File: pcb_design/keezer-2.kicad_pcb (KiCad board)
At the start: 2 copper layers, 27.9 x 39.4 mm, 10 parts, among them Q1 PN2222A, T1 CONN_01X03_FEMALE, T2 CONN_01X03_FEMALE, T3 CONN_01X03_FEMALE

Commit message: Wire everything up in the pcb
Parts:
- moved R2 12.7 mm to (172.7, 129.5)
- moved Q1 2.84 mm to (156.2, 119.4), turned to 90 degrees
- moved R1 2.54 mm to (158.8, 130.8)
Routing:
- net GND: track 0.00 -> 96.1 mm
- net +3V3: track 0.00 -> 88.0 mm
- net BCM4: track 0.00 -> 68.6 mm, vias 0 -> 1
- net +5V: track 0.00 -> 38.2 mm
- net SCL: track 0.00 -> 29.0 mm
- net SDA: track 0.00 -> 25.7 mm
- net RELAY_OUT: track 0.00 -> 16.6 mm
- net BCM17: track 0.00 -> 10.7 mm
- net TRANSISTOR_BASE: track 0.00 -> 8.89 mm
- removed copper zone on F.Cu, net +3V3
- removed copper zone on F.Cu, net +5V
- removed copper zone on B.Cu, net GND
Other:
- board size 27.9 x 39.4 mm -> 29.2 x 39.4 mm
- rule trace_min: 0.2 -> 0.1524

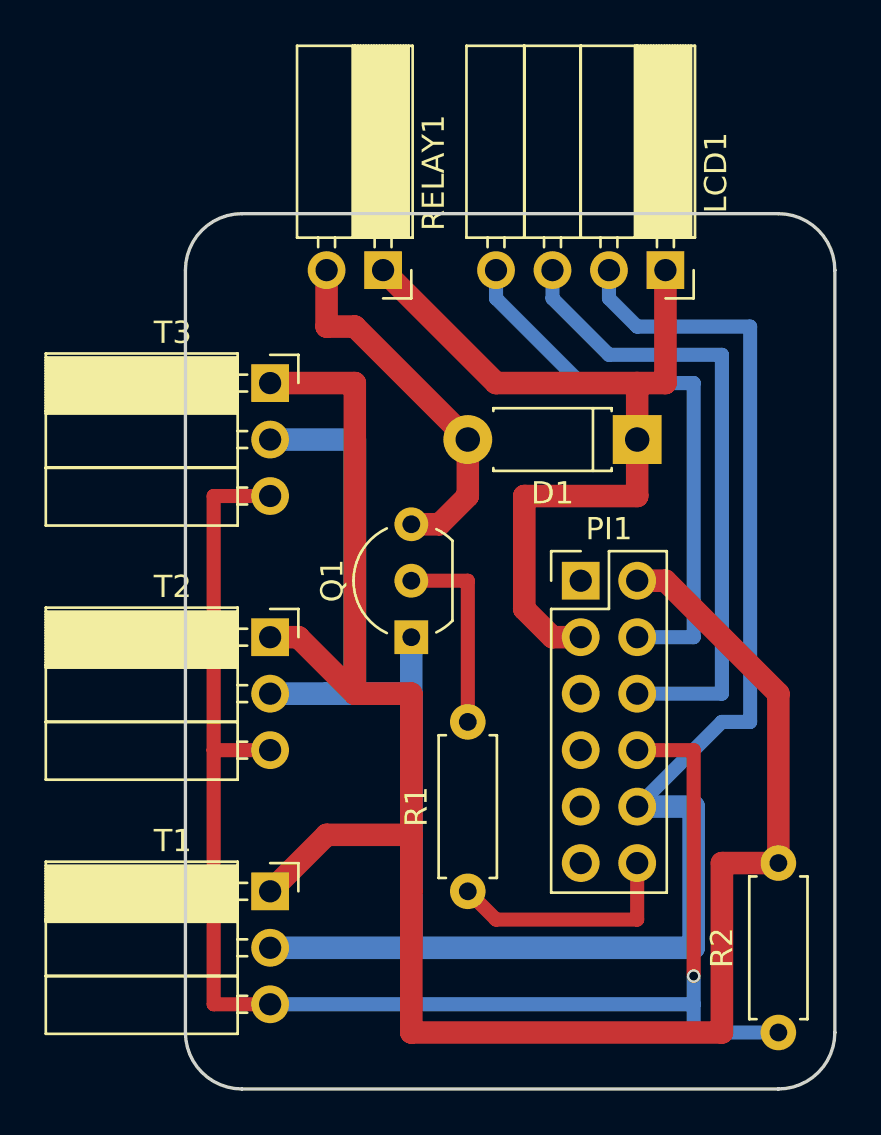
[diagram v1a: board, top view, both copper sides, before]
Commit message: Fix some silkscreen; fill bottom layer with ground zone
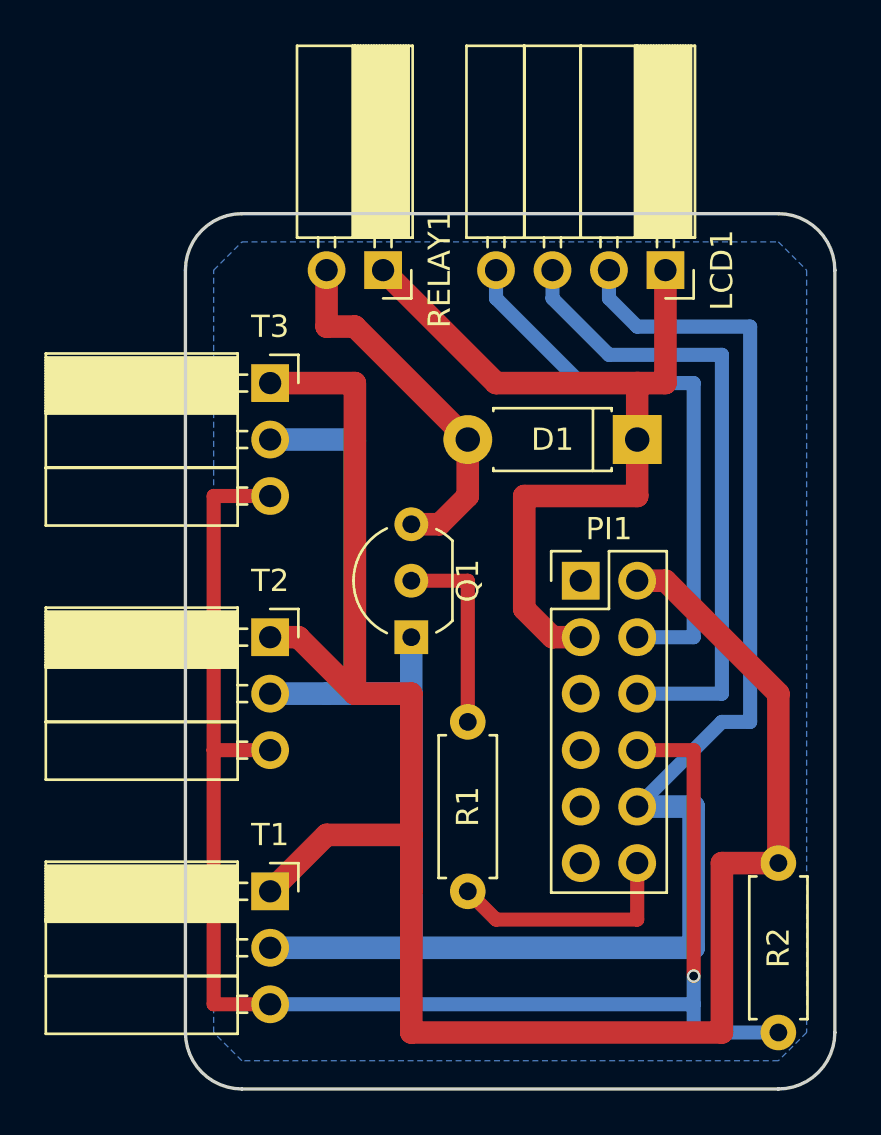
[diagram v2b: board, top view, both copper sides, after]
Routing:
- added copper zone on B.Cu, net GND
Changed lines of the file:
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@@
     (links 22)
     (no_connects 0)
-    (area 137.327619 90.337618 175.335001 139.775001)
+    (area 145.974999 100.254999 175.335001 139.775001)
     (thickness 1.6)
     (drawings 8)
@@
   (layers
     (0 F.Cu signal)
-    (31 B.Cu signal hide)
+    (31 B.Cu signal)
     (32 B.Adhes user)
     (33 F.Adhes user)
@@
     (pad_to_mask_clearance 0.2)
     (aux_axis_origin 0 0)
-    (visible_elements 7FFCFFFF)
+    (visible_elements 7FFEFFFF)
     (pcbplotparams
       (layerselection 0x00030_80000001)
@@
     (descr "D, DO-41_SOD81 series, Axial, Horizontal, pin pitch=7.62mm, , length*diameter=5.2*2.7mm^2, , http://www.diodes.com/_files/packages/DO-41%20(Plastic).pdf")
     (tags "D DO-41_SOD81 series Axial Horizontal pin pitch 7.62mm  length 5.2mm diameter 2.7mm")
-    (fp_text reference D1 (at 3.81 -2.41 180) (layer F.SilkS)
+    (fp_text reference D1 (at 3.81 0 180) (layer F.SilkS)
       (effects (font (size 1 1) (thickness 0.15)))
     )
@@
     (descr "Through hole angled socket strip, 1x04, 2.54mm pitch, 8.51mm socket length, single row")
     (tags "Through hole angled socket strip THT 1x04 2.54mm single row")
-    (fp_text reference LCD1 (at -4.38 -2.27 270) (layer F.SilkS)
+    (fp_text reference LCD1 (at 0 -2.54 270) (layer F.SilkS)
       (effects (font (size 1 1) (thickness 0.15)))
     )
@@
     (descr "TO-92 leads in-line, wide, drill 0.8mm (see NXP sot054_po.pdf)")
     (tags "to-92 sc-43 sc-43a sot54 PA33 transistor")
-    (fp_text reference Q1 (at 2.54 -3.56 270) (layer F.SilkS)
+    (fp_text reference Q1 (at 2.54 2.54 270) (layer F.SilkS)
       (effects (font (size 1 1) (thickness 0.15)))
     )
@@
       (effects (font (size 1 1) (thickness 0.15)))
     )
-    (fp_text user %R (at 2.54 -3.56 270) (layer F.Fab)
+    (fp_text user %R (at 2.54 2.54 270) (layer F.Fab)
       (effects (font (size 1 1) (thickness 0.15)))
     )
@@
     (descr "Resistor, Axial_DIN0207 series, Axial, Horizontal, pin pitch=7.62mm, 0.25W = 1/4W, length*diameter=6.3*2.5mm^2, http://cdn-reichelt.de/documents/datenblatt/B400/1_4W%23YAG.pdf")
     (tags "Resistor Axial_DIN0207 series Axial Horizontal pin pitch 7.62mm 0.25W = 1/4W length 6.3mm diameter 2.5mm")
-    (fp_text reference R1 (at 3.81 -2.31 90) (layer F.SilkS)
+    (fp_text reference R1 (at 3.81 0 90) (layer F.SilkS)
       (effects (font (size 1 1) (thickness 0.15)))
     )
@@
     (descr "Resistor, Axial_DIN0207 series, Axial, Horizontal, pin pitch=7.62mm, 0.25W = 1/4W, length*diameter=6.3*2.5mm^2, http://cdn-reichelt.de/documents/datenblatt/B400/1_4W%23YAG.pdf")
     (tags "Resistor Axial_DIN0207 series Axial Horizontal pin pitch 7.62mm 0.25W = 1/4W length 6.3mm diameter 2.5mm")
-    (fp_text reference R2 (at 3.81 2.54 270) (layer F.SilkS)
+    (fp_text reference R2 (at 3.81 0 270) (layer F.SilkS)
       (effects (font (size 1 1) (thickness 0.15)))
     )
@@
     (descr "Through hole angled socket strip, 1x02, 2.54mm pitch, 8.51mm socket length, single row")
     (tags "Through hole angled socket strip THT 1x02 2.54mm single row")
-    (fp_text reference RELAY1 (at -4.38 -2.27 270) (layer F.SilkS)
+    (fp_text reference RELAY1 (at 0 -2.54 270) (layer F.SilkS)
       (effects (font (size 1 1) (thickness 0.15)))
     )
@@
     (descr "Through hole angled socket strip, 1x03, 2.54mm pitch, 8.51mm socket length, single row")
     (tags "Through hole angled socket strip THT 1x03 2.54mm single row")
-    (fp_text reference T1 (at -4.38 -2.27) (layer F.SilkS)
+    (fp_text reference T1 (at 0 -2.54) (layer F.SilkS)
       (effects (font (size 1 1) (thickness 0.15)))
     )
@@
     (descr "Through hole angled socket strip, 1x03, 2.54mm pitch, 8.51mm socket length, single row")
     (tags "Through hole angled socket strip THT 1x03 2.54mm single row")
-    (fp_text reference T2 (at -4.38 -2.27) (layer F.SilkS)
+    (fp_text reference T2 (at 0 -2.54) (layer F.SilkS)
       (effects (font (size 1 1) (thickness 0.15)))
     )
@@
     (descr "Through hole angled socket strip, 1x03, 2.54mm pitch, 8.51mm socket length, single row")
     (tags "Through hole angled socket strip THT 1x03 2.54mm single row")
-    (fp_text reference T3 (at -4.38 -2.27) (layer F.SilkS)
+    (fp_text reference T3 (at 0 -2.54) (layer F.SilkS)
       (effects (font (size 1 1) (thickness 0.15)))
     )
@@
   (segment (start 157.48 114.3) (end 158.75 113.03) (width 1.016) (layer F.Cu) (net 2))
   (segment (start 153.67 121.92) (end 153.67 110.49) (width 1.016) (layer B.Cu) (net 3))
-  (segment (start 153.67 110.49) (end 149.86 110.49) (width 1.016) (layer B.Cu) (net 3) (status 800000))
+  (segment (start 153.67 110.49) (end 149.86 110.49) (width 1.016) (layer B.Cu) (net 3))
   (segment (start 156.21 121.92) (end 156.21 133.35) (width 1.016) (layer B.Cu) (net 3))
   (segment (start 149.86 121.92) (end 152.4 121.92) (width 1.016) (layer B.Cu) (net 3))
@@
   (segment (start 172.72 121.92) (end 172.72 129.54) (width 1.016) (layer F.Cu) (net 6))
   (segment (start 167.64 116.84) (end 172.72 121.92) (width 1.016) (layer F.Cu) (net 6))
-  (segment (start 147.32 124.46) (end 149.86 124.46) (width 0.635) (layer F.Cu) (net 9) (status 800000))
-  (segment (start 149.86 135.89) (end 168.91 135.89) (width 0.635) (layer B.Cu) (net 9) (status 400000))
-  (segment (start 149.86 135.89) (end 147.32 135.89) (width 0.635) (layer F.Cu) (net 9) (status 400000))
-  (segment (start 147.32 113.03) (end 149.86 113.03) (width 0.635) (layer F.Cu) (net 9) (status 800000))
+  (segment (start 147.32 124.46) (end 149.86 124.46) (width 0.635) (layer F.Cu) (net 9))
+  (segment (start 149.86 135.89) (end 168.91 135.89) (width 0.635) (layer B.Cu) (net 9))
+  (segment (start 149.86 135.89) (end 147.32 135.89) (width 0.635) (layer F.Cu) (net 9))
+  (segment (start 147.32 113.03) (end 149.86 113.03) (width 0.635) (layer F.Cu) (net 9))
   (segment (start 147.32 135.89) (end 147.32 124.46) (width 0.635) (layer F.Cu) (net 9))
   (segment (start 147.32 124.46) (end 147.32 113.03) (width 0.635) (layer F.Cu) (net 9))
@@
   (segment (start 158.75 123.19) (end 158.75 116.84) (width 0.635) (layer F.Cu) (net 13))
   (segment (start 158.75 116.84) (end 156.21 116.84) (width 0.635) (layer F.Cu) (net 13))
+  (zone (net 3) (net_name GND) (layer B.Cu) (hatch edge 0.508)
+    (connect_pads (clearance 0.508))
+    (min_thickness 0.254)
+    (fill yes (arc_segments 16) (thermal_gap 0.508) (thermal_bridge_width 0.508))
+    (polygon
+      (pts
+        (xy 173.99 102.87) (xy 173.99 137.16) (xy 172.72 138.43) (xy 148.59 138.43) (xy 147.32 137.16)
+        (xy 147.32 102.87) (xy 148.59 101.6) (xy 172.72 101.6)
+      )
+    )
+  )
 )

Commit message: Add more silkscreen
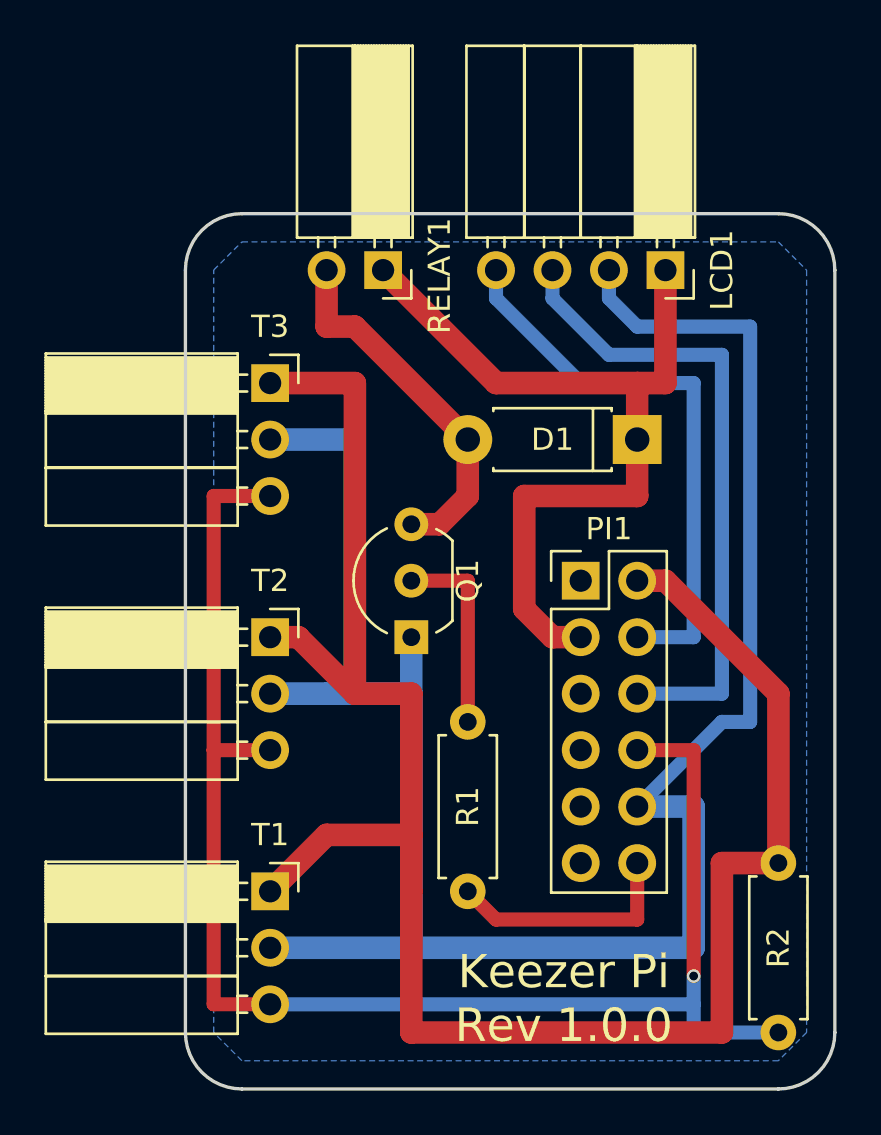
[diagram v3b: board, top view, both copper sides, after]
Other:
- board text added: "+"
- board text added: "+5v"
- board text added: "-"
- board text added: "DQ"
- board text added: "GND"
- board text added: "Keezer Pi Rev 1.0.0"
- board text added: "LCD1"
- board text added: "RELAY1"
- board text added: "SCL"
- board text added: "SDA"
- board text added: "T1"
- board text added: "T2"
- board text added: "T3"
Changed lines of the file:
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@@
     (area 145.974999 100.254999 175.335001 139.775001)
     (thickness 1.6)
-    (drawings 8)
+    (drawings 29)
     (tracks 77)
     (zones 0)
@@
   )
   (setup
-    (last_trace_width 1.016)
+    (last_trace_width 0.25)
     (user_trace_width 0.254)
     (user_trace_width 0.635)
@@
     (descr "Through hole angled socket strip, 1x02, 2.54mm pitch, 8.51mm socket length, single row")
     (tags "Through hole angled socket strip THT 1x02 2.54mm single row")
-    (fp_text reference RELAY1 (at 0 -2.54 270) (layer F.SilkS)
+    (fp_text reference RELAY1 (at 0.254 -2.54 270) (layer F.SilkS)
       (effects (font (size 1 1) (thickness 0.15)))
     )
@@
     (fp_line (start -10.55 4.35) (end -10.55 -1.8) (layer F.CrtYd) (width 0.05))
     (fp_line (start -10.55 -1.8) (end 1.8 -1.8) (layer F.CrtYd) (width 0.05))
-    (fp_text user %R (at 0 -2.54 270) (layer F.Fab)
+    (fp_text user %R (at 0.254 -2.54 270) (layer F.Fab)
       (effects (font (size 1 1) (thickness 0.15)))
     )
@@
     )
   )
+  (gr_text T1 (at 149.86 128.27) (layer B.SilkS)
+    (effects (font (size 1.016 1.016) (thickness 0.127)) (justify mirror))
+  )
+  (gr_text T2 (at 149.86 116.84) (layer B.SilkS)
+    (effects (font (size 1.016 1.016) (thickness 0.127)) (justify mirror))
+  )
+  (gr_text T3 (at 149.86 105.41) (layer B.SilkS)
+    (effects (font (size 1.016 1.016) (thickness 0.127)) (justify mirror))
+  )
+  (gr_text RELAY1 (at 157.48 103.124 90) (layer B.SilkS)
+    (effects (font (size 1.016 1.016) (thickness 0.127)) (justify mirror))
+  )
+  (gr_text "LCD1\n" (at 171.196 102.87) (layer B.SilkS)
+    (effects (font (size 1.016 1.016) (thickness 0.127)) (justify mirror))
+  )
+  (gr_text "Keezer Pi\nRev 1.0.0" (at 163.068 135.636) (layer F.SilkS)
+    (effects (font (size 1.5 1.5) (thickness 0.3)))
+  )
+  (gr_text DQ (at 151.638 135.89) (layer B.SilkS)
+    (effects (font (size 0.762 0.762) (thickness 0.1524)) (justify mirror))
+  )
+  (gr_text - (at 151.638 133.35) (layer B.SilkS)
+    (effects (font (size 0.762 0.762) (thickness 0.1524)) (justify mirror))
+  )
+  (gr_text + (at 151.638 130.81) (layer B.SilkS)
+    (effects (font (size 0.762 0.762) (thickness 0.1524)) (justify mirror))
+  )
+  (gr_text DQ (at 151.638 124.46) (layer B.SilkS)
+    (effects (font (size 0.762 0.762) (thickness 0.1524)) (justify mirror))
+  )
+  (gr_text - (at 151.638 121.92) (layer B.SilkS)
+    (effects (font (size 0.762 0.762) (thickness 0.1524)) (justify mirror))
+  )
+  (gr_text + (at 151.638 119.38) (layer B.SilkS)
+    (effects (font (size 0.762 0.762) (thickness 0.1524)) (justify mirror))
+  )
+  (gr_text DQ (at 151.638 113.03) (layer B.SilkS)
+    (effects (font (size 0.762 0.762) (thickness 0.1524)) (justify mirror))
+  )
+  (gr_text - (at 151.638 110.49) (layer B.SilkS)
+    (effects (font (size 0.762 0.762) (thickness 0.1524)) (justify mirror))
+  )
+  (gr_text + (at 151.638 107.95) (layer B.SilkS)
+    (effects (font (size 0.762 0.762) (thickness 0.1524)) (justify mirror))
+  )
+  (gr_text GND (at 152.4 104.648) (layer B.SilkS)
+    (effects (font (size 0.762 0.762) (thickness 0.1524)) (justify mirror))
+  )
+  (gr_text +5v (at 155.194 104.648) (layer B.SilkS)
+    (effects (font (size 0.762 0.762) (thickness 0.1524)) (justify mirror))
+  )
+  (gr_text +5v (at 167.894 104.648) (layer B.SilkS)
+    (effects (font (size 0.762 0.762) (thickness 0.1524)) (justify mirror))
+  )
+  (gr_text GND (at 165.1 104.648) (layer B.SilkS)
+    (effects (font (size 0.762 0.762) (thickness 0.1524)) (justify mirror))
+  )
+  (gr_text SCL (at 162.56 104.648) (layer B.SilkS)
+    (effects (font (size 0.762 0.762) (thickness 0.1524)) (justify mirror))
+  )
+  (gr_text SDA (at 160.02 104.648) (layer B.SilkS)
+    (effects (font (size 0.762 0.762) (thickness 0.1524)) (justify mirror))
+  )
   (gr_arc (start 148.59 102.87) (end 146.05 102.87) (angle 90) (layer Edge.Cuts) (width 0.15))

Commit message: Update pcb design to match OSH Park's minimum requirements
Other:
- net class Default: clearance 0.2 -> 0.1524; trace_width 0.25 -> 0.1524; via_dia 0.6 -> 0.6858; via_drill 0.4 -> 0.3302
- rule trace_clearance: 0.2 -> 0.1524
- rule via_min_drill: 0.3 -> 0.3302
- rule via_min_size: 0.4 -> 0.6858
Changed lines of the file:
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@@
   )
   (setup
-    (last_trace_width 0.25)
+    (last_trace_width 0.1524)
     (user_trace_width 0.254)
     (user_trace_width 0.635)
     (user_trace_width 1.016)
-    (trace_clearance 0.2)
+    (trace_clearance 0.1524)
     (zone_clearance 0.508)
     (zone_45_only no)
@@
     (segment_width 0.2)
     (edge_width 0.15)
-    (via_size 0.6)
-    (via_drill 0.4)
-    (via_min_size 0.4)
-    (via_min_drill 0.3)
-    (uvia_size 0.3)
-    (uvia_drill 0.1)
+    (via_size 0.6858)
+    (via_drill 0.3302)
+    (via_min_size 0.6858)
+    (via_min_drill 0.3302)
+    (uvia_size 0.762)
+    (uvia_drill 0.508)
     (uvias_allowed no)
     (uvia_min_size 0.2)
@@
   (net 14 "Net-(PI1-Pad1)")
   (net_class Default "This is the default net class."
-    (clearance 0.2)
-    (trace_width 0.25)
-    (via_dia 0.6)
-    (via_drill 0.4)
-    (uvia_dia 0.3)
-    (uvia_drill 0.1)
+    (clearance 0.1524)
+    (trace_width 0.1524)
+    (via_dia 0.6858)
+    (via_drill 0.3302)
+    (uvia_dia 0.762)
+    (uvia_drill 0.508)
     (add_net +3V3)
     (add_net +5V)
